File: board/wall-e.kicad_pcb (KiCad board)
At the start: 2 copper layers, 78.7 x 64.4 mm, 64 parts, among them J1 Raspberry_Pi_2_3, J10 PCA9685, J11 VL53L0X, J12 VL53L0X, J13 VL53L0X, J14 MotorDrv2, J15 Motor2, J16 IMU, J17 INA219, J18 INA219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

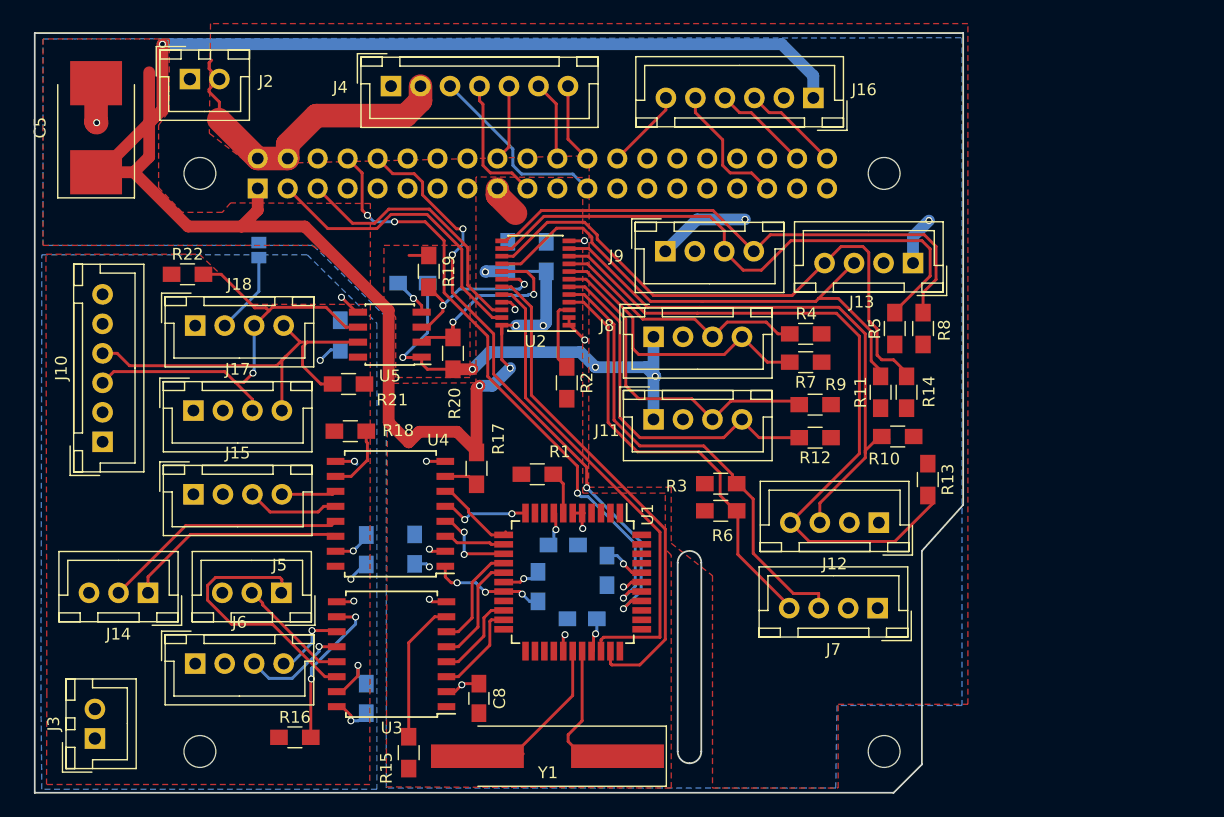
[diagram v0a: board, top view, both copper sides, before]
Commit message: Swap in through-hole cap
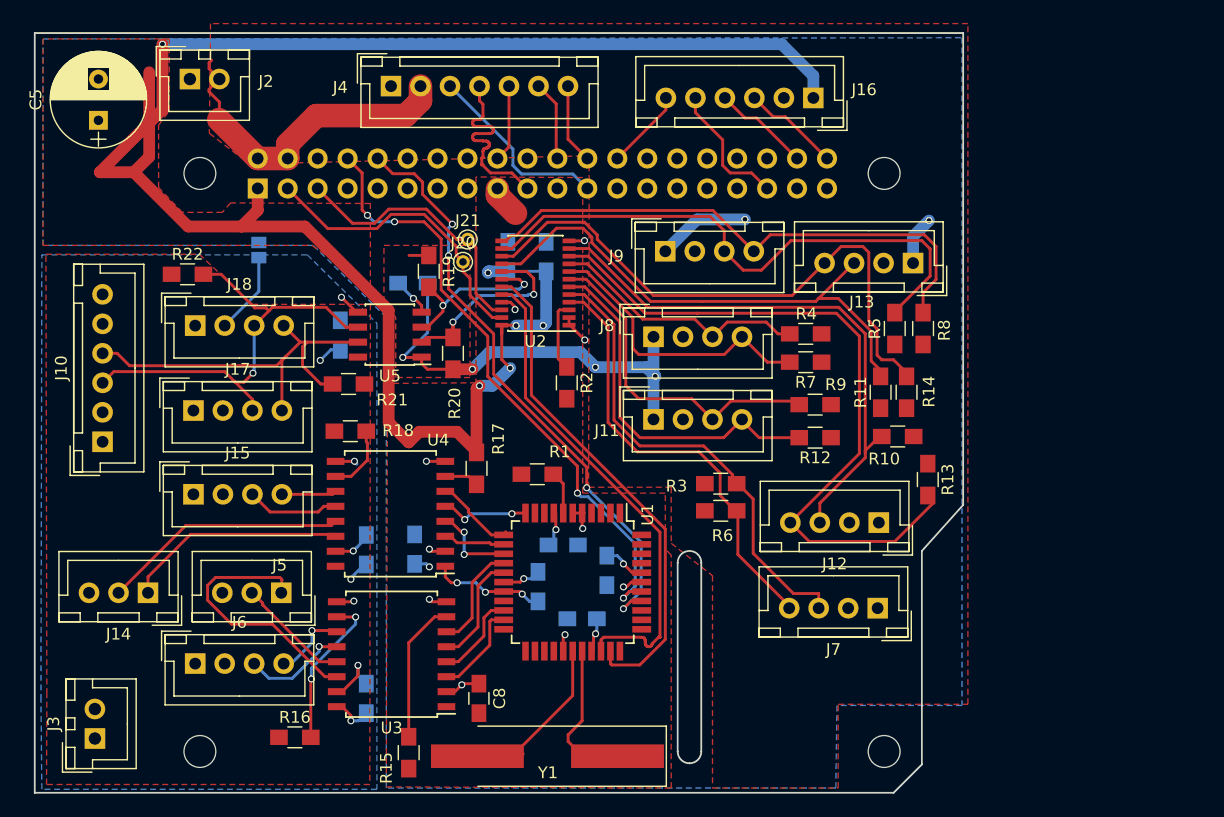
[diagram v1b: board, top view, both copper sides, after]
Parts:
- added J20: SDA, Connectors:PINTST, F.Cu at (82.9, 34.2)
- added J21: SCL, Connectors:PINTST, F.Cu at (83.3, 32.3)
- C5: footprint Capacitors_Tantalum_SMD:CP_Tantalum_Case-E_EIA-7260-38_Hand -> Capacitors_THT:CP_Radial_D8.0mm_P3.50mm
- moved C5 0.66 mm to (52.0, 22.2)
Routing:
- net PI_SPI_MOSI: track 11.4 -> 16.7 mm
- net GND: track 28.4 -> 25.0 mm, vias 13 -> 12
- net PI_I2C_SCLK: track 22.7 -> 23.8 mm
- net I2C_M7_SCLK: track 41.1 -> 42.0 mm
- net PI_RX: track 52.0 -> 51.2 mm
- net +3V3: track 183.3 -> 182.5 mm

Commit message: Move board over ports and re-route.
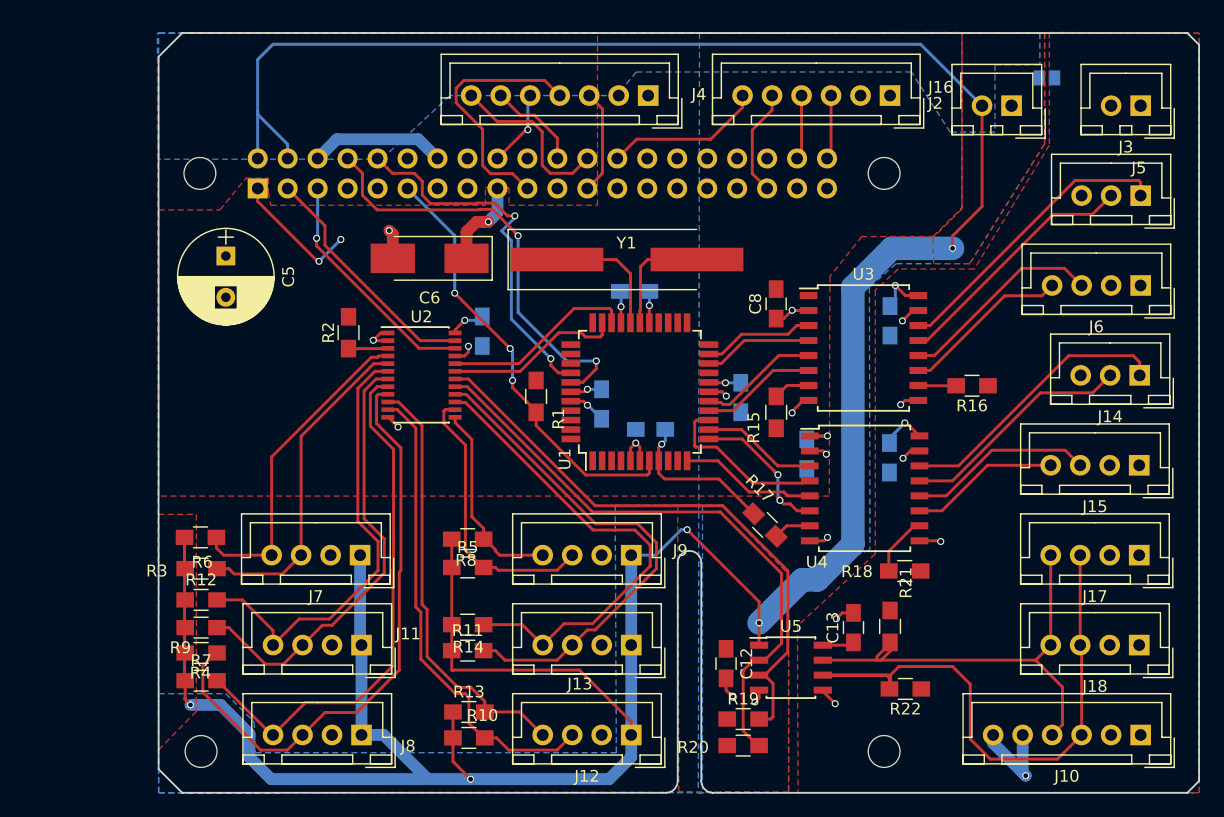
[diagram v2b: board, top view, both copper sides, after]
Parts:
- removed J20: SDA, Connectors:PINTST
- removed J21: SCL, Connectors:PINTST
- C12, C13: moved to F.Cu
- C6: footprint Capacitors_SMD:C_0805_HandSoldering -> Capacitors_Tantalum_SMD:CP_Tantalum_Case-C_EIA-6032-28_Hand; moved to F.Cu
- moved J3 103.6 mm to (140.4, 21.0), turned to 180 degrees
- moved J10 91.4 mm to (140.4, 74.3), turned to 180 degrees
- moved J6 86.3 mm to (140.4, 36.2), turned to 180 degrees
- moved J14 86.1 mm to (140.3, 43.9)
- moved J18 84.5 mm to (140.3, 66.7), turned to 180 degrees
- moved J17 81.1 mm to (140.3, 59.1), turned to 180 degrees
- moved J5 80.2 mm to (140.4, 28.6)
- moved J15 80.2 mm to (140.3, 51.5), turned to 180 degrees
- moved R22 70.3 mm to (120.4, 70.4), turned to 180 degrees
- moved J2 69.7 mm to (129.4, 21.0), turned to 180 degrees
- moved J19 68.4 mm to (132.4, 18.6), turned to 90 degrees
- moved R16 64.7 mm to (126.1, 44.7), turned to 180 degrees
- moved R4 58.0 mm to (60.7, 67.4), turned to 0 degrees
- moved R7 57.9 mm to (60.7, 69.7), turned to 0 degrees
- moved R9 55.4 mm to (60.7, 65.2), turned to 0 degrees
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- renumbered REF** to ?
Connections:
- J1 pad 11: Net-(J1-Pad11) -> PROP_RES
- J1 pad 12: Net-(J1-Pad12) -> (no net)
- J1 pad 13: Net-(J1-Pad13) -> (no net)
- J1 pad 15: Net-(J1-Pad15) -> (no net)
- J1 pad 16: Net-(J1-Pad16) -> (no net)
- J1 pad 21: PI_SPI_MISO -> (no net)
- J1 pad 27: Net-(J1-Pad27) -> (no net)
- J1 pad 28: Net-(J1-Pad28) -> (no net)
- J1 pad 29: Net-(J1-Pad29) -> (no net)
- J1 pad 31: Net-(J1-Pad31) -> (no net)
- J1 pad 32: Net-(J1-Pad32) -> (no net)
- J1 pad 33: Net-(J1-Pad33) -> (no net)
- J1 pad 36: Net-(J1-Pad36) -> (no net)
- J1 pad 37: Net-(J1-Pad37) -> (no net)
- J1 pad 7: Net-(J1-Pad7) -> (no net)
- J4 pad 2: +5V -> +3V3
- U1 pad 1: Net-(U1-Pad1) -> (no net)
- U1 pad 10: Net-(U1-Pad10) -> (no net)
- U1 pad 19: Net-(U1-Pad19) -> (no net)
- U1 pad 2: Net-(U1-Pad2) -> (no net)
- U1 pad 22: PROP_SERV1 -> (no net)
- U1 pad 23: PROP_SERV2 -> (no net)
- U1 pad 24: PROP_SERV3 -> (no net)
- U1 pad 25: PROP_SERV4 -> (no net)
- U1 pad 26: Net-(U1-Pad26) -> (no net)
- U1 pad 3: Net-(U1-Pad3) -> (no net)
- U1 pad 33: M4_DIR -> (no net)
- U1 pad 34: M4_PWM -> (no net)
- U1 pad 35: M4_ENCB -> (no net)
- U1 pad 36: M4_ENCA -> (no net)
- U1 pad 4: Net-(U1-Pad4) -> (no net)
- U1 pad 41: M1_ENCB -> (no net)
- U1 pad 42: M1_ENCA -> (no net)
- U1 pad 43: M1_PWM -> (no net)
- U1 pad 44: M1_DIR -> (no net)
- U1 pad 9: Net-(U1-Pad9) -> (no net)
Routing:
- net +5V: track 80.3 -> 286.9 mm, vias 6 -> 5
- net +3V3: track 182.5 -> 47.1 mm, vias 13 -> 9
- net I2C_M6_SCLK: track 14.6 -> 50.2 mm, vias 2 -> 0
- net I2C_M6_SDA: track 17.0 -> 51.3 mm, vias 2 -> 0
- net PROP_RES: track 3.67 -> 37.1 mm, vias 0 -> 3
- net I2C_M4_SDA: track 46.5 -> 17.0 mm
- net I2C_M2_SCLK: track 22.2 -> 50.8 mm
- net I2C_M7_SDA: track 42.7 -> 15.1 mm
- net I2C_M7_SCLK: track 42.0 -> 16.3 mm
- net I2C_M4_SCLK: track 48.3 -> 23.9 mm
- net I2C_M3_SDA: track 59.8 -> 36.6 mm
- net I2C_M2_SDA: track 24.7 -> 44.9 mm
- net PI_RX: track 51.2 -> 31.2 mm, vias 4 -> 2
- net GND: track 25.0 -> 41.1 mm, vias 12 -> 14
- net PI_TX: track 52.4 -> 36.4 mm, vias 4 -> 2
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- added copper zone on B.Cu, net +5V
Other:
- board size 78.7 x 64.4 mm -> 88.2 x 64.4 mm

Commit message: Tweaks
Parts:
- moved ? 0.10 mm to (60.6, 75.7)
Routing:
- net PI_SPI_MOSI: track 21.7 -> 11.0 mm
- net PI_SPI_SCLK: track 8.87 -> 11.4 mm
- net Net-(J5-Pad1): track 25.1 -> 26.9 mm
- net I2C_M0_SCLK: track 28.0 -> 29.7 mm
- net PI_SPI_CE0: track 14.8 -> 16.3 mm

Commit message: Update silkscreen
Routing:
- net +3V3: track 47.1 -> 58.7 mm, vias 9 -> 13
- net I2C_ISO_SDA: track 39.1 -> 37.3 mm
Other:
- board text added: "D.PWR"
- board text added: "IMU"
- board text added: "LOGIC PWR"
- board text added: "M.DRV"
- board text added: "M.SIG"
- board text added: "PWR MON"
- board text added: "SCREEN"
- board text added: "SENSORS"
- board text added: "SERVO"

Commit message: Tweaks: add cap and fill.
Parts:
- added C14: 10u, Capacitors_Tantalum_SMD:CP_Tantalum_Case-C_EIA-6032-28_Hand, F.Cu at (79.5, 73.3)
- moved R14 1.30 mm to (83.4, 63.7)
- moved R11 1.30 mm to (83.4, 65.9)
- moved R10 0.72 mm to (84.1, 74.7)
- moved R13 0.72 mm to (84.1, 72.5)
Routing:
- net GND: track 41.1 -> 44.0 mm, vias 14 -> 15
- net +5V: track 286.8 -> 284.6 mm, vias 5 -> 6
- net I2C_M5_SCLK: track 42.8 -> 43.9 mm
- net I2C_M3_SDA: track 36.6 -> 35.6 mm
